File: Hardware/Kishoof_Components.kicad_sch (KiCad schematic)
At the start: 98 parts, among them J1 Conn_01x12_Pin, J2 Conn_01x12_Pin, J3 Conn_01x12_Pin, J4 Conn_01x12_Pin, J5 Eurorack_10_pin_power, J6 SWD_Header, J7 Conn_01x02_Pin, U1 STM32H7B0VBTx, U2 PCM5100APW, U3 TPS561201, U4 LT1117-3.3, U5 MCP6002, U6 MX25LM51245G, U7 MCP6004, U8 TL072, Y1 8MHz 20pF

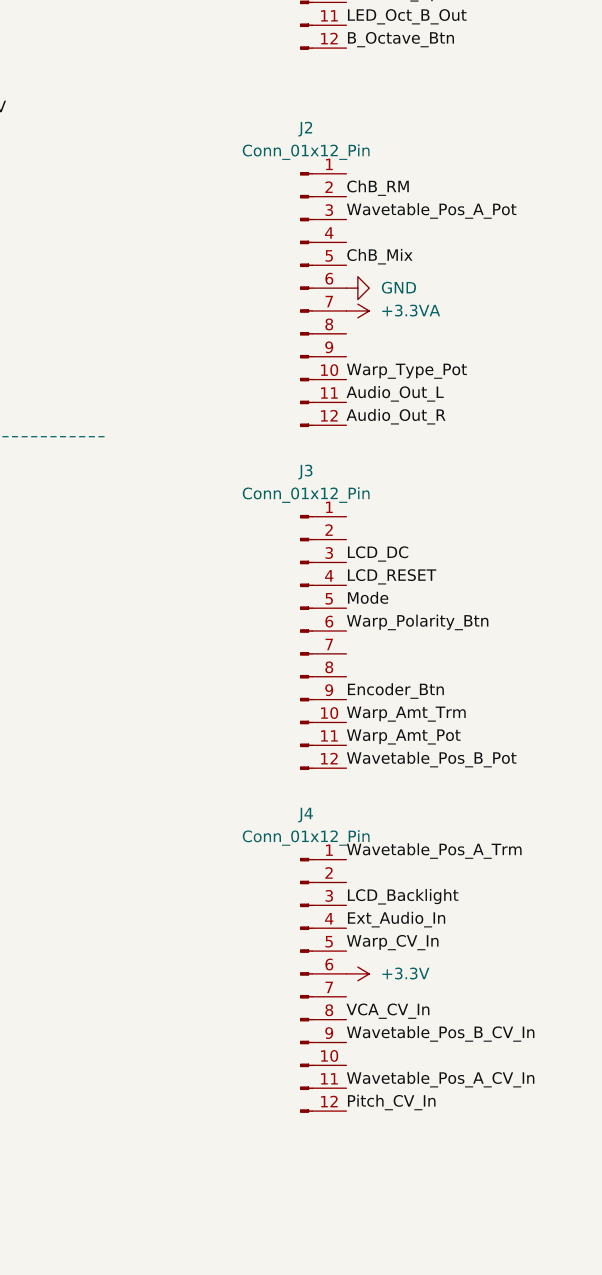
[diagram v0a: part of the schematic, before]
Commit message: First pass of component board routing complete
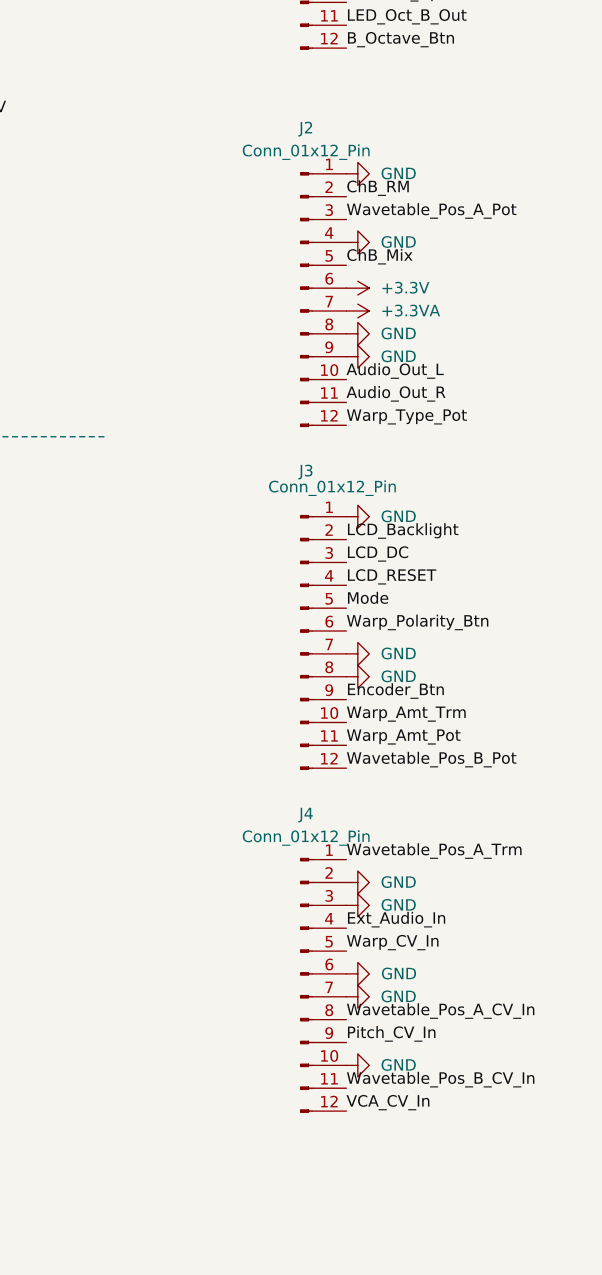
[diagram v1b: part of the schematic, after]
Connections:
- net +3.3V: now also J2.6 (Pin_6); no longer J4.6 (Pin_6)
- net Audio_Out_L: now also J2.10 (Pin_10); no longer J2.11 (Pin_11)
- net Audio_Out_R: now also J2.11 (Pin_11); no longer J2.12 (Pin_12)
- net GND: now also J2.1 (Pin_1), J2.4 (Pin_4), J2.8 (Pin_8), J2.9 (Pin_9), J3.1 (Pin_1), J3.7 (Pin_7), J3.8 (Pin_8), J4.10 (Pin_10), J4.2 (Pin_2), J4.3 (Pin_3), J4.6 (Pin_6), J4.7 (Pin_7); no longer J2.6 (Pin_6)
- net LCD_Backlight: now also J3.2 (Pin_2); no longer J4.3 (Pin_3)
- net Pitch_CV_In: now also J4.9 (Pin_9); no longer J4.12 (Pin_12)
- net VCA_CV_In: now also J4.12 (Pin_12); no longer J4.8 (Pin_8)
- net Warp_Type_Pot: now also J2.12 (Pin_12); no longer J2.10 (Pin_10)
- net Wavetable_Pos_A_CV_In: now also J4.8 (Pin_8); no longer J4.11 (Pin_11)
- net Wavetable_Pos_B_CV_In: now also J4.11 (Pin_11); no longer J4.9 (Pin_9)

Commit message: Cleaned up inter-board connectors
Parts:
- added NT2: NetTie_2, symbol Device:NetTie_2
- J3: renamed from J2; value Conn_01x12_Pin -> Conn_01x10_Pin; footprint Connector_PinHeader_2.54mm:PinHeader_1x12_P2.54mm_Vertical -> Connector_PinHeader_2.54mm:PinHeader_1x10_P2.54mm_Vertical; symbol Connector:Conn_01x12_Pin -> Connector:Conn_01x10_Pin
- J4: value Conn_01x12_Pin -> Conn_01x10_Pin; footprint Connector_PinHeader_2.54mm:PinHeader_1x12_P2.54mm_Vertical -> Connector_PinHeader_2.54mm:PinHeader_1x10_P2.54mm_Vertical; symbol Connector:Conn_01x12_Pin -> Connector:Conn_01x10_Pin
- renumbered J3 to J2
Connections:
- net +3.3V: now also J3.5 (Pin_5); no longer J3.6 (Pin_6)
- net +3.3VA: now also J3.6 (Pin_6); no longer J3.7 (Pin_7)
- net Audio_Out_L: now also J3.8 (Pin_8); no longer J3.10 (Pin_10)
- net Audio_Out_R: now also J3.9 (Pin_9); no longer J3.11 (Pin_11)
- net ChB_Mix: now also J3.4 (Pin_4); no longer J3.5 (Pin_5)
- net ChB_RM: now also J3.1 (Pin_1); no longer J3.2 (Pin_2)
- net Ext_Audio_In: now also J4.3 (Pin_3); no longer J4.4 (Pin_4)
- net GND: now also J1.2 (Pin_2), J1.6 (Pin_6), J3.3 (Pin_3), J3.7 (Pin_7), J4.5 (Pin_5), J4.8 (Pin_8), NT2.2; no longer J2.1 (Pin_1), J2.8 (Pin_8), J3.1 (Pin_1), J3.4 (Pin_4), J3.8 (Pin_8), J3.9 (Pin_9), J4.10 (Pin_10), J4.3 (Pin_3), J4.6 (Pin_6), J4.7 (Pin_7), U1.32 (PC4)
- net LCD_Backlight: now also J2.1 (Pin_1); no longer J2.2 (Pin_2)
- net LCD_DC: now also J2.4 (Pin_4); no longer J2.3 (Pin_3)
- net LCD_RESET: now also J2.5 (Pin_5); no longer J2.4 (Pin_4)
- net LCD_SPI3_MOSI: now also J1.1 (Pin_1); no longer J1.3 (Pin_3)
- net LCD_SPI3_SCK: now also J1.3 (Pin_3); no longer J1.4 (Pin_4)
- net LCD_SPI3_SS: now also J1.4 (Pin_4); no longer J1.5 (Pin_5)
- net Mode: now also J2.6 (Pin_6); no longer J2.5 (Pin_5)
- net Octave_Down: now also J2.3 (Pin_3); no longer J1.1 (Pin_1)
- net Octave_Up: now also J2.2 (Pin_2); no longer J1.2 (Pin_2)
- net Pitch_CV_In: now also J4.7 (Pin_7); no longer J4.9 (Pin_9)
- net USB_DP: now also J1.5 (Pin_5); no longer J1.6 (Pin_6)
- net VCA_CV_In: now also J4.10 (Pin_10); no longer J4.12 (Pin_12)
- net Warp_CV_In: now also J4.4 (Pin_4); no longer J4.5 (Pin_5)
- net Warp_Polarity_Btn: now also J2.8 (Pin_8); no longer J2.6 (Pin_6)
- net Warp_Type_Pot: now also J3.10 (Pin_10); no longer J3.12 (Pin_12)
- net Wavetable_Pos_A_CV_In: now also J4.6 (Pin_6); no longer J4.8 (Pin_8)
- net Wavetable_Pos_A_Pot: now also J3.2 (Pin_2); no longer J3.3 (Pin_3)
- net Wavetable_Pos_B_CV_In: now also J4.9 (Pin_9); no longer J4.11 (Pin_11)
- new net: NT2.1, U1.32 (PC4)
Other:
- moved on the sheet: J2

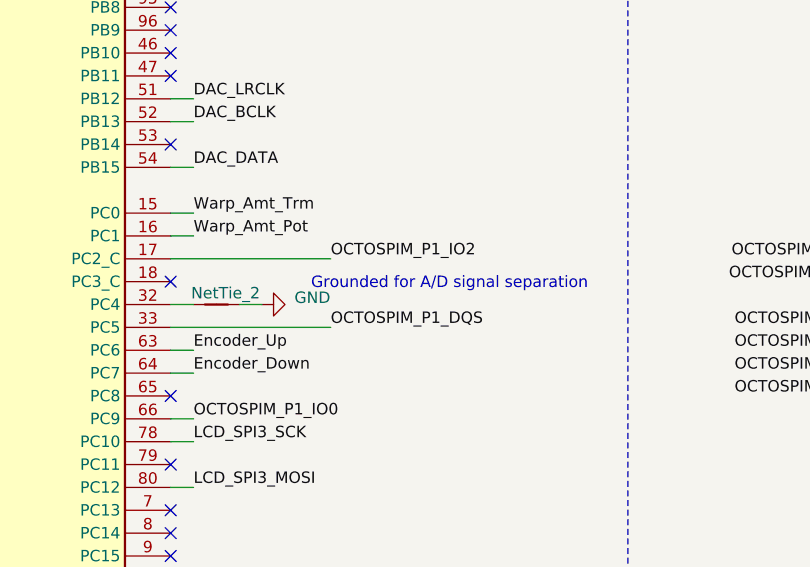
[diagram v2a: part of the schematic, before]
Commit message: Control board routed; updated lcd riser
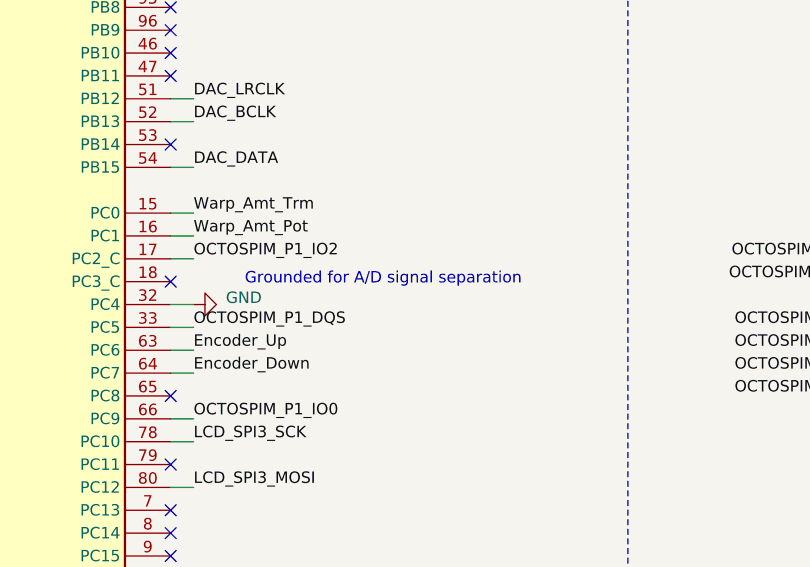
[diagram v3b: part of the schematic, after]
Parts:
- removed NT2: NetTie_2, symbol Device:NetTie_2
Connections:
- net GND: now also U1.32 (PC4)
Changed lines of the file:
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@@
 	(wire
 		(pts
-			(xy 113.03 146.05) (xy 130.81 146.05)
+			(xy 113.03 146.05) (xy 115.57 146.05)
 		)
 		(stroke
@@
 	(wire
 		(pts
-			(xy 113.03 138.43) (xy 130.81 138.43)
+			(xy 113.03 138.43) (xy 115.57 138.43)
 		)
 		(stroke
@@
 	(wire
 		(pts
-			(xy 120.65 143.51) (xy 123.19 143.51)
-		)
-		(stroke
-			(width 0)
-			(type default)
-		)
-	)
-	(wire
-		(pts
 			(xy 36.83 35.56) (xy 36.83 38.1)
 		)
@@
 	(text "Grounded for A/D signal separation"
 		(exclude_from_sim no)
-		(at 144.018 141.224 0)
+		(at 136.652 140.716 0)
 		(effects
 			(font
@@
 	)
 	(label "OCTOSPIM_P1_DQS"
-		(at 130.81 146.05 0)
+		(at 115.57 146.05 0)
 		(fields_autoplaced yes)
 		(effects
@@
 	)
 	(label "OCTOSPIM_P1_IO2"
-		(at 130.81 138.43 0)
+		(at 115.57 138.43 0)
 		(fields_autoplaced yes)
 		(effects
@@
 	)
 	(symbol
-		(lib_id "Device:NetTie_2")
-		(at 118.11 143.51 0)
-		(unit 1)
-		(exclude_from_sim no)
-		(in_bom no)
-		(on_board yes)
-		(dnp no)
-		(property "Reference" "NT2"
-			(at 119.38 140.208 0)
-			(effects
-				(font
-					(size 1.27 1.27)
-				)
-				(hide yes)
-			)
-		)
-		(property "Value" "NetTie_2"
-			(at 119.126 142.24 0)
-			(effects
-				(font
-					(size 1.27 1.27)
-				)
-			)
-		)
-		(property "Footprint" ""
-			(at 118.11 143.51 0)
-			(effects
-				(font
-					(size 1.27 1.27)
-				)
-				(hide yes)
-			)
-		)
-		(property "Datasheet" "~"
-			(at 118.11 143.51 0)
-			(effects
-				(font
-					(size 1.27 1.27)
-				)
-				(hide yes)
-			)
-		)
-		(property "Description" "Net tie, 2 pins"
-			(at 118.11 143.51 0)
-			(effects
-				(font
-					(size 1.27 1.27)
-				)
-				(hide yes)
-			)
-		)
-		(pin "2"
-		)
-		(pin "1"
-		)
-		(instances
-			(project "Kishoof_Components"
-				(path "/00778401-a8b8-4a7c-bae7-c4fa7505df01"
-					(reference "NT2")
-					(unit 1)
-				)
-			)
-		)
-	)
-	(symbol
 		(lib_id "Device:R_Small")
 		(at 185.42 260.35 0)
@@
 	(symbol
 		(lib_id "power:GND")
-		(at 123.19 143.51 90)
+		(at 115.57 143.51 90)
 		(unit 1)
 		(exclude_from_sim no)
@@
 		(dnp no)
 		(property "Reference" "#PWR091"
-			(at 129.54 143.51 0)
+			(at 121.92 143.51 0)
 			(effects
 				(font
@@
 		)
 		(property "Value" "GND"
-			(at 128.778 142.748 90)
+			(at 121.158 142.748 90)
 			(effects
 				(font
@@
 		)
 		(property "Footprint" ""
-			(at 123.19 143.51 0)
+			(at 115.57 143.51 0)
 			(effects
 				(font
@@
 		)
 		(property "Datasheet" ""
-			(at 123.19 143.51 0)
+			(at 115.57 143.51 0)
 			(effects
 				(font
@@
 		)
 		(property "Description" "Power symbol creates a global label with name \"GND\" , ground"
-			(at 123.19 143.51 0)
+			(at 115.57 143.51 0)
 			(effects
 				(font

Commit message: PCBs v1.0 ordered
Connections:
- net GND: now also U5.5 (+), U8.3 (+), U8.5 (+); no longer U5.6 (-), U8.2 (-), U8.6 (-)
- net at C35.2, R22.1, R23.1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: now also U5.6 (-); no longer U5.5 (+)
- net at C32.2, R6.1, R8.2: now also U8.6 (-); no longer U8.5 (+)
- net at C31.2, R5.1, R7.2: now also U8.2 (-); no longer U8.3 (+)
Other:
- note added: "Connectors"
- note removed: "ADC Pins -------- PA0 ADC1_INP16 PA1 ADC1_INP17 PA2 ADC12_INP14 PA3 ADC12_INP15 [PA4 ADC12_INP18 DAC] [PA5 ADC12_INP19 DAC] PA6 ADC12_INP3 PA7 ADC12_INP7 PB0 ADC12_INP9 PB1 ADC12_INP5 PC0 ADC123_INP10 PC1 ADC123_INP11 PC2 ADC123_INP12 [PC3_C ADC3_INP1] PC4 ADC12_INP4 PC5 ADC12_INP8 PF11 ADC1_INP2 PF12 ADC1_INP6 PF13 ADC2_INP2 PF14 ADC2_INP6"
- note removed: "Protection and Output"
- moved on the sheet: C1, C2, C36, C5, C6, C7, C8, C9, D1, D2, D3, J1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

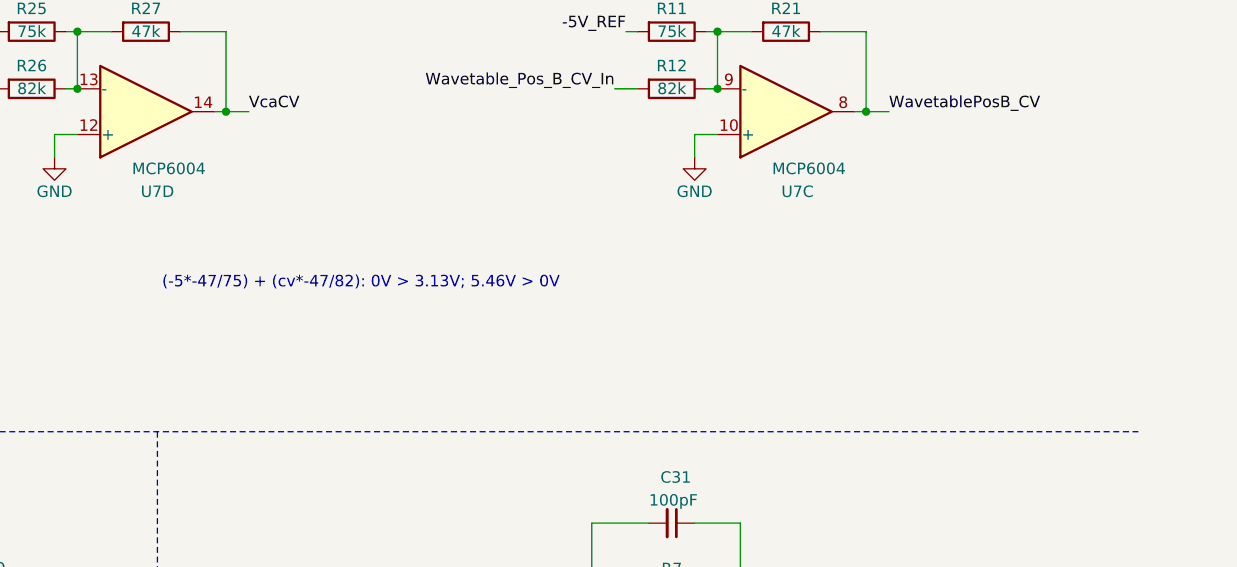
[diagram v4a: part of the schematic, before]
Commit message: Fixed issue refreshing wavetable list after USB deletion
Started adding support for fragmented wavetables
Fixes for directory printing formatting
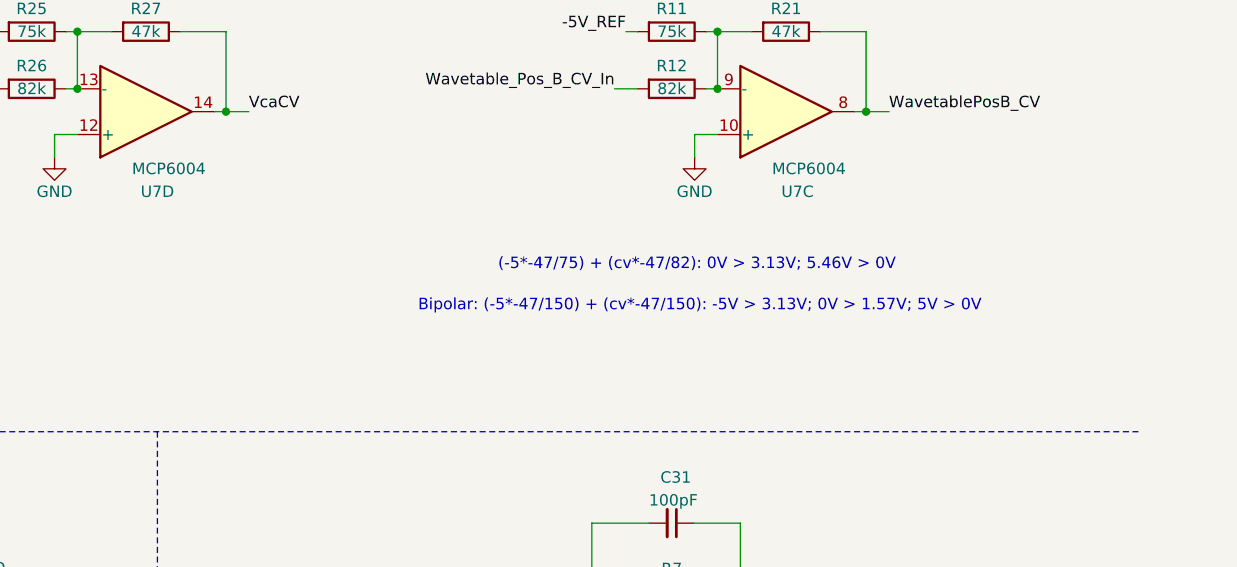
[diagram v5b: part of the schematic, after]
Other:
- note added: "Bipolar: (-5*-47/150) + (cv*-47/150): -5V > 3.13V; 0V > 1.57V; 5V > 0V"
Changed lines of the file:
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@@
 	(text "(-5*-47/75) + (cv*-47/82): 0V > 3.13V; 5.46V > 0V\n"
 		(exclude_from_sim no)
-		(at 300.228 132.842 0)
+		(at 337.566 130.81 0)
 		(effects
 			(font
@@
 		(effects
 			(font
+				(size 1.27 1.27)
+			)
+			(justify left bottom)
+		)
+	)
+	(text "Bipolar: (-5*-47/150) + (cv*-47/150): -5V > 3.13V; 0V > 1.57V; 5V > 0V\n"
+		(exclude_from_sim no)
+		(at 328.676 135.382 0)
+		(effects
+			(font
